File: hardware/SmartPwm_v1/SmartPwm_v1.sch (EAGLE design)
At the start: 12 parts, among them IC1 7805T, Q1 IRF3704-H, Q2 IRF3704-H, U1 ICL7667CPAZ

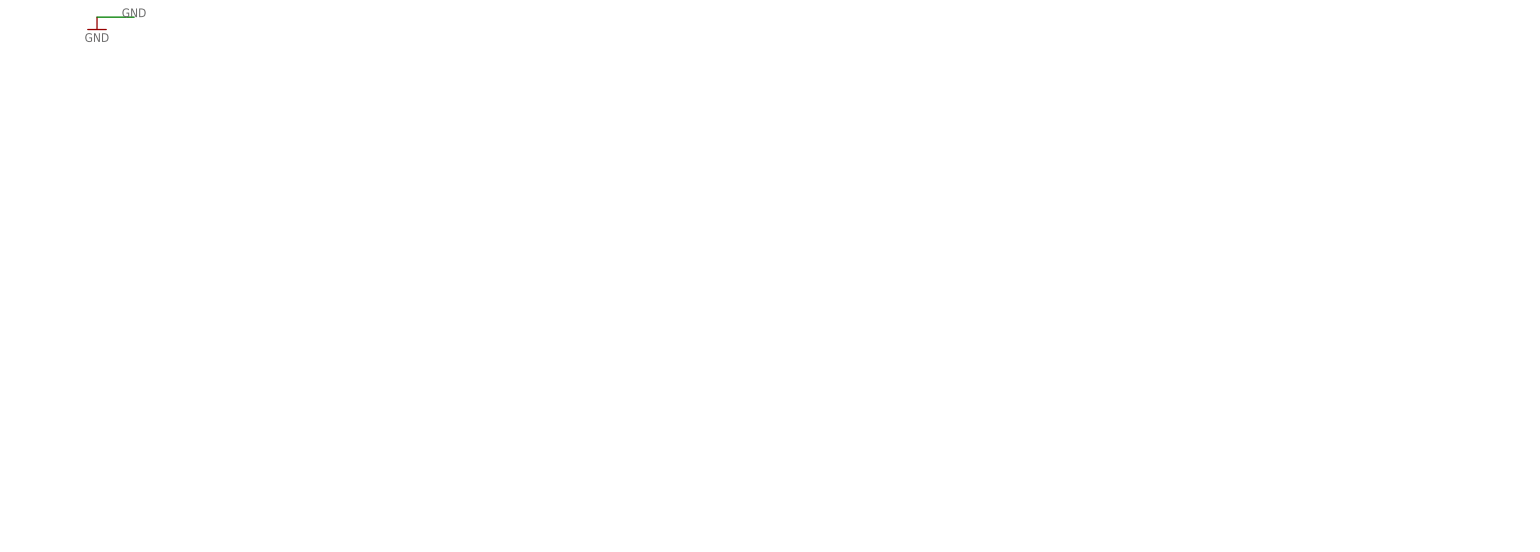
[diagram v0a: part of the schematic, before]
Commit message: add esp32 headers to shematic, add 4 control lines for pwm
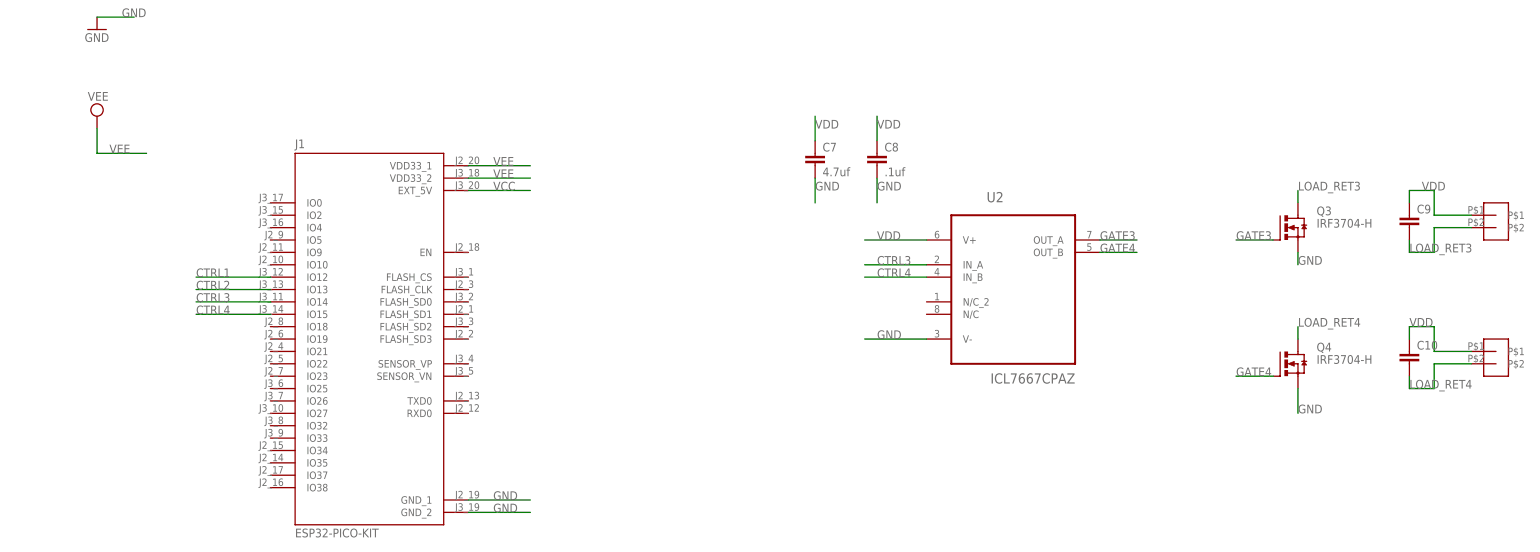
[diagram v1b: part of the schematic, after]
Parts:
- added C10, C9: (no value), capacitor-wima:C2.5/2
- added C7: 4.7uf, capacitor-wima:C2.5/2
- added C8: .1uf, capacitor-wima:C2.5/2
- added J1: ESP32-PICO-KIT, ESP32-PICO-KIT:ESP32-PICO-KIT
- added Q3, Q4: IRF3704-H, transistor-power:IRF3704-H
- added U$3, U$4: TB002-500-P02, mylib:TB002-500-P02
- added U2: ICL7667CPAZ, ICL7667CPAZ:ICL7667CPAZ
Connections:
- new net CTRL3: J1.IO14, U2.IN_A
- new net CTRL4: J1.IO15, U2.IN_B
- new net GATE3: Q3.G, U2.OUT_A
- new net GATE4: Q4.G, U2.OUT_B
- new net LOAD_RET3: C9.2, Q3.D, U$3.P$2
- new net LOAD_RET4: C10.2, Q4.D, U$4.P$2
- new net VEE: J1.VDD33_1, J1.VDD33_2
- net CTRL1: now also J1.IO12
- net CTRL2: now also J1.IO13
- net GND: now also C7.2, C8.2, J1.GND_1, J1.GND_2, Q3.S, Q4.S, U2.V-
- net VCC: now also J1.EXT_5V
- net VDD: now also C10.1, C7.1, C8.1, C9.1, U$3.P$1, U$4.P$1, U2.V+

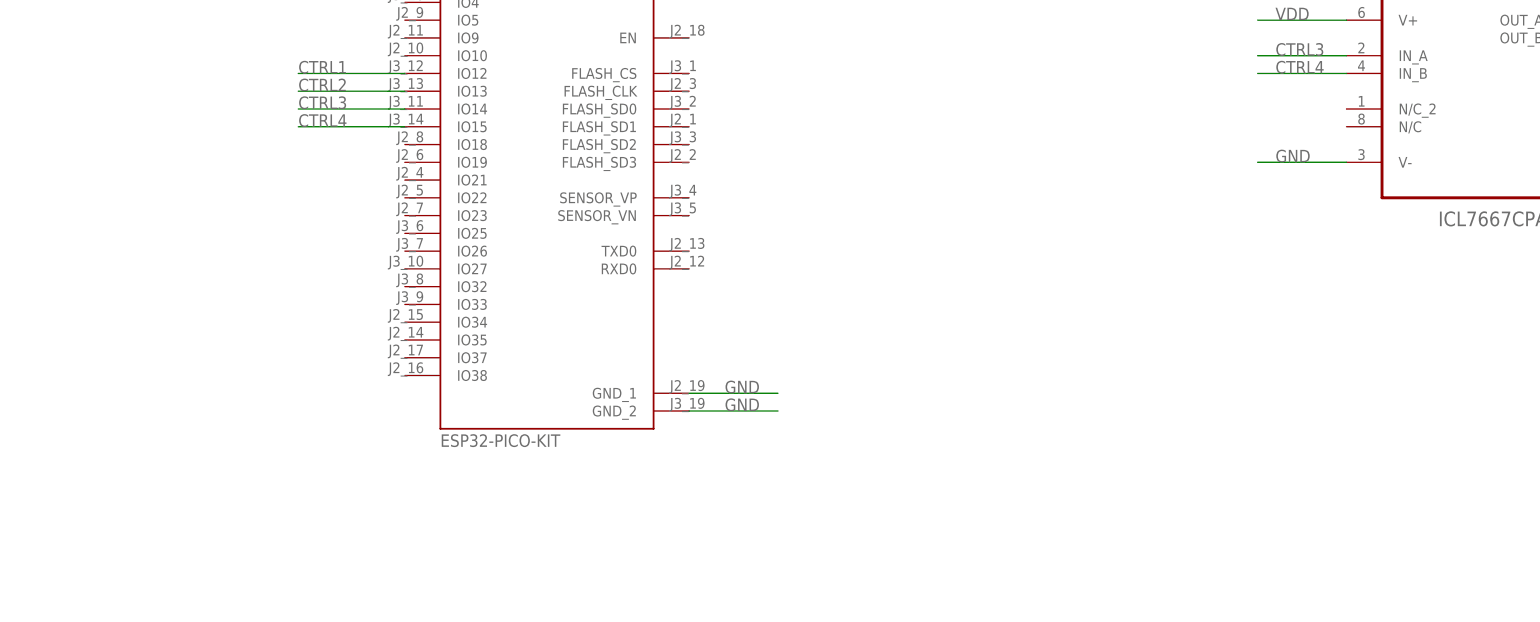
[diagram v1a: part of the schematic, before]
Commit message: Add header for IIC LCD display and add dht11 temp sensor
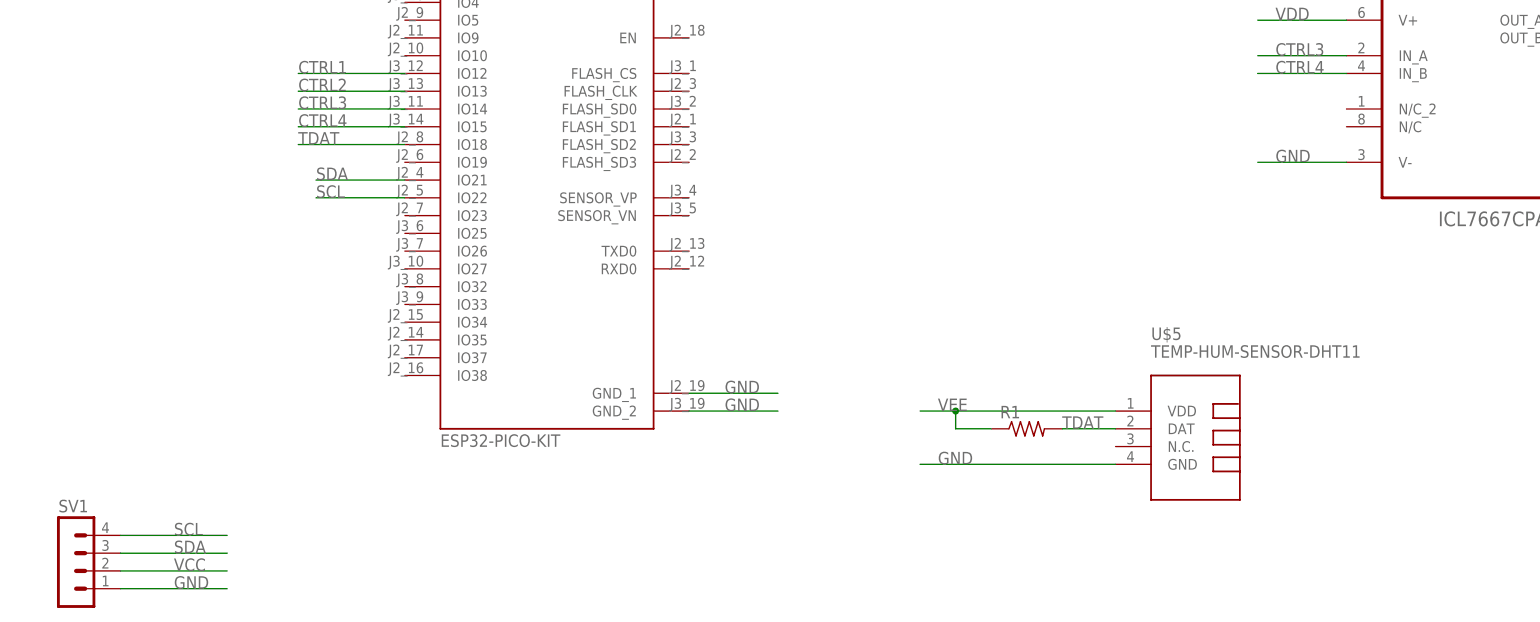
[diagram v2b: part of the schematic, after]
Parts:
- added R1: (no value), rcl:R-US_0207/10
- added SV1: (no value), con-lstb:MA04-1
- added U$5: TEMP-HUM-SENSOR-DHT11, diy-modules:TEMP-HUM-SENSOR-DHT11
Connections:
- new net SCL: J1.IO22, SV1.4
- new net SDA: J1.IO21, SV1.3
- new net TDAT: J1.IO18, R1.2, U$5.DAT
- net GND: now also SV1.1, U$5.GND
- net VCC: now also SV1.2
- net VEE: now also R1.1, U$5.VDD
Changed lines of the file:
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@@
 <layer number="97" name="Info" color="7" fill="1" visible="yes" active="yes"/>
 <layer number="98" name="Guide" color="6" fill="1" visible="yes" active="yes"/>
+<layer number="101" name="Hidden" color="15" fill="1" visible="yes" active="yes"/>
+<layer number="102" name="Changes" color="12" fill="1" visible="yes" active="yes"/>
 </layers>
 <schematic xreflabel="%F%N/%S.%C%R" xrefpart="/%S.%C%R">
@@
 <part name="C9" library="capacitor-wima" library_urn="urn:adsk.eagle:library:116" deviceset="C" device="2.5/2" package3d_urn="urn:adsk.eagle:package:5415/1"/>
 <part name="C10" library="capacitor-wima" library_urn="urn:adsk.eagle:library:116" deviceset="C" device="2.5/2" package3d_urn="urn:adsk.eagle:package:5415/1"/>
+<part name="SV1" library="con-lstb" library_urn="urn:adsk.eagle:library:162" deviceset="MA04-1" device="" package3d_urn="urn:adsk.eagle:package:8337/1"/>
+<part name="U$5" library="diy-modules" deviceset="TEMP-HUM-SENSOR-DHT11" device=""/>
+<part name="R1" library="rcl" library_urn="urn:adsk.eagle:library:334" deviceset="R-US_" device="0207/10" package3d_urn="urn:adsk.eagle:package:23491/2"/>
 </parts>
 <sheets>
@@
 <attribute name="VALUE" x="286.004" y="-22.479" size="1.778" layer="96"/>
 </instance>
+<instance part="SV1" gate="1" x="2.54" y="-71.12" smashed="yes">
+<attribute name="VALUE" x="1.27" y="-81.28" size="1.778" layer="96"/>
+<attribute name="NAME" x="1.27" y="-65.278" size="1.778" layer="95"/>
+</instance>
+<instance part="U$5" gate="G$1" x="165.1" y="-55.88" smashed="yes">
+<attribute name="NAME" x="157.48" y="-40.64" size="1.778" layer="95"/>
+<attribute name="VALUE" x="157.48" y="-43.18" size="1.778" layer="95"/>
+</instance>
+<instance part="R1" gate="G$1" x="139.7" y="-53.34" smashed="yes">
+<attribute name="NAME" x="135.89" y="-51.8414" size="1.778" layer="95"/>
+<attribute name="VALUE" x="135.89" y="-56.642" size="1.778" layer="96"/>
+</instance>
 </instances>
 <busses>
@@
 <label x="175.26" y="15.24" size="1.778" layer="95"/>
 </segment>
+<segment>
+<pinref part="SV1" gate="1" pin="1"/>
+<wire x1="10.16" y1="-76.2" x2="25.4" y2="-76.2" width="0.1524" layer="91"/>
+<label x="17.78" y="-76.2" size="1.778" layer="95"/>
+</segment>
+<segment>
+<pinref part="U$5" gate="G$1" pin="GND"/>
+<wire x1="152.4" y1="-58.42" x2="124.46" y2="-58.42" width="0.1524" layer="91"/>
+<label x="127" y="-58.42" size="1.778" layer="95"/>
+</segment>
 </net>
 <net name="VCC" class="0">
@@
 <pinref part="J1" gate="G$1" pin="EXT_5V"/>
 <label x="96.52" y="15.24" size="1.778" layer="95"/>
+</segment>
+<segment>
+<pinref part="SV1" gate="1" pin="2"/>
+<wire x1="10.16" y1="-73.66" x2="25.4" y2="-73.66" width="0.1524" layer="91"/>
+<label x="17.78" y="-73.66" size="1.778" layer="95"/>
 </segment>
 </net>
@@
 <label x="96.52" y="17.78" size="1.778" layer="95"/>
 </segment>
+<segment>
+<pinref part="U$5" gate="G$1" pin="VDD"/>
+<wire x1="152.4" y1="-50.8" x2="129.54" y2="-50.8" width="0.1524" layer="91"/>
+<pinref part="R1" gate="G$1" pin="1"/>
+<wire x1="134.62" y1="-53.34" x2="129.54" y2="-53.34" width="0.1524" layer="91"/>
+<wire x1="129.54" y1="-53.34" x2="129.54" y2="-50.8" width="0.1524" layer="91"/>
+<wire x1="129.54" y1="-50.8" x2="124.46" y2="-50.8" width="0.1524" layer="91"/>
+<junction x="129.54" y="-50.8"/>
+<label x="127" y="-50.8" size="1.778" layer="95"/>
+</segment>
 </net>
 <net name="CTRL4" class="0">
@@
 <wire x1="261.62" y1="12.7" x2="261.62" y2="15.24" width="0.1524" layer="91"/>
 <label x="261.62" y="15.24" size="1.778" layer="95"/>
+</segment>
+</net>
+<net name="SCL" class="0">
+<segment>
+<pinref part="SV1" gate="1" pin="4"/>
+<wire x1="10.16" y1="-68.58" x2="25.4" y2="-68.58" width="0.1524" layer="91"/>
+<label x="17.78" y="-68.58" size="1.778" layer="95"/>
+</segment>
+<segment>
+<pinref part="J1" gate="G$1" pin="IO22"/>
+<wire x1="50.8" y1="-20.32" x2="38.1" y2="-20.32" width="0.1524" layer="91"/>
+<label x="38.1" y="-20.32" size="1.778" layer="95"/>
+</segment>
+</net>
+<net name="SDA" class="0">
+<segment>
+<pinref part="SV1" gate="1" pin="3"/>
+<wire x1="10.16" y1="-71.12" x2="25.4" y2="-71.12" width="0.1524" layer="91"/>
+<label x="17.78" y="-71.12" size="1.778" layer="95"/>
+</segment>
+<segment>
+<pinref part="J1" gate="G$1" pin="IO21"/>
+<wire x1="50.8" y1="-17.78" x2="38.1" y2="-17.78" width="0.1524" layer="91"/>
+<label x="38.1" y="-17.78" size="1.778" layer="95"/>
+</segment>
+</net>
+<net name="TDAT" class="0">
+<segment>
+<pinref part="U$5" gate="G$1" pin="DAT"/>
+<pinref part="R1" gate="G$1" pin="2"/>
+<wire x1="152.4" y1="-53.34" x2="144.78" y2="-53.34" width="0.1524" layer="91"/>
+<label x="144.78" y="-53.34" size="1.778" layer="95"/>
+</segment>
+<segment>
+<pinref part="J1" gate="G$1" pin="IO18"/>
+<wire x1="50.8" y1="-12.7" x2="35.56" y2="-12.7" width="0.1524" layer="91"/>
+<label x="35.56" y="-12.7" size="1.778" layer="95"/>
 </segment>
 </net>
@@
 packages will not be understood (or retained) with this version.
 </note>
+<note version="8.4" severity="warning">
+Since Version 8.4, EAGLE supports properties for SPICE simulation.
+Probes in schematics and SPICE mapping objects found in parts and library devices
+will not be understood with this version. Update EAGLE to the latest version
+for full support of SPICE simulation.
+</note>
 </compatibility>

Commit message: add knobs to schematic, rearrange ios, select lcd and add to docs
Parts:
- added MT1, MT2, MT3, MT4, MT5: PEC11R-4215F-S0024, PEC11R-4215F-S0024:PEC11R-4215F-S0024
- added R2: 10M, rcl:R-US_0207/10
- added R3: 1M, rcl:R-US_0207/10
- added R4, R5: 10K, rcl:R-US_0207/10
- added SV2: (no value), con-lstb:MA04-1
- added U$6: 74AHTC125, DIP794W45P254L1969H508Q14:74AHTC125
- C10, C5, C6, C9: value (none) -> 10uf
- R1: value (none) -> 10K
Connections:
- new net K1_A: J1.IO2, MT1.A
- new net K1_B: J1.IO5, MT1.B
- new net K1_S: J1.IO0, MT1.2
- new net K2_A: J1.IO26, MT2.A
- new net K2_B: J1.IO10, MT2.B
- new net K2_S: J1.IO4, MT2.2
- new net K3_A: J1.IO32, MT3.A
- new net K3_B: J1.IO9, MT3.B
- new net K3_S: J1.IO27, MT3.2
- new net K4_A: J1.IO35, MT4.A
- new net K4_B: MT4.B
- new net K4_S: J1.IO34, MT4.2
- new net K5_A: J1.IO33, MT5.A
- new net K5_B: J1.IO25, MT5.B
- new net K5_S: J1.IO37, MT5.2
- new net LDAT3V3: J1.IO19, U$6.1A
- new net LDAT5V: SV2.2, SV2.3, U$6.1Y
- new net VDIV: J1.IO38, R2.1, R3.2
- net GND: now also MT1.1, MT1.COM, MT1.SHIELD, MT2.1, MT2.COM, MT2.SHIELD, MT3.1, MT3.COM, MT3.SHIELD, MT4.1, MT4.COM, MT4.SHIELD, MT5.1, MT5.COM, MT5.SHIELD, R3.1, SV2.1, U$6.1OE_N, U$6.2A, U$6.3A, U$6.GND
- net SCL: now also R4.2
- net SDA: now also R5.2
- net VCC: now also U$6.2OE_N, U$6.3OE_N, U$6.4A, U$6.4OE_N, U$6.VCC; no longer SV1.2
- net VDD: now also R2.2, SV2.4
- net VEE: now also R4.1, R5.1, SV1.2
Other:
- note added: "ADC_CH2"
- note added: "LCD Display"
- note added: "Optional pullups, do not populate if not needed"
- note added: "PWM Outputs"
- note added: "Power Monitor"
- note added: "RTC_GPIO"
- note added: "Temperature"
- note added: "VEE = 3v3"
- note added: "knobs"
- note added: "lowimpedance"
- note added: "tantalum"
- note added: "ws2815"

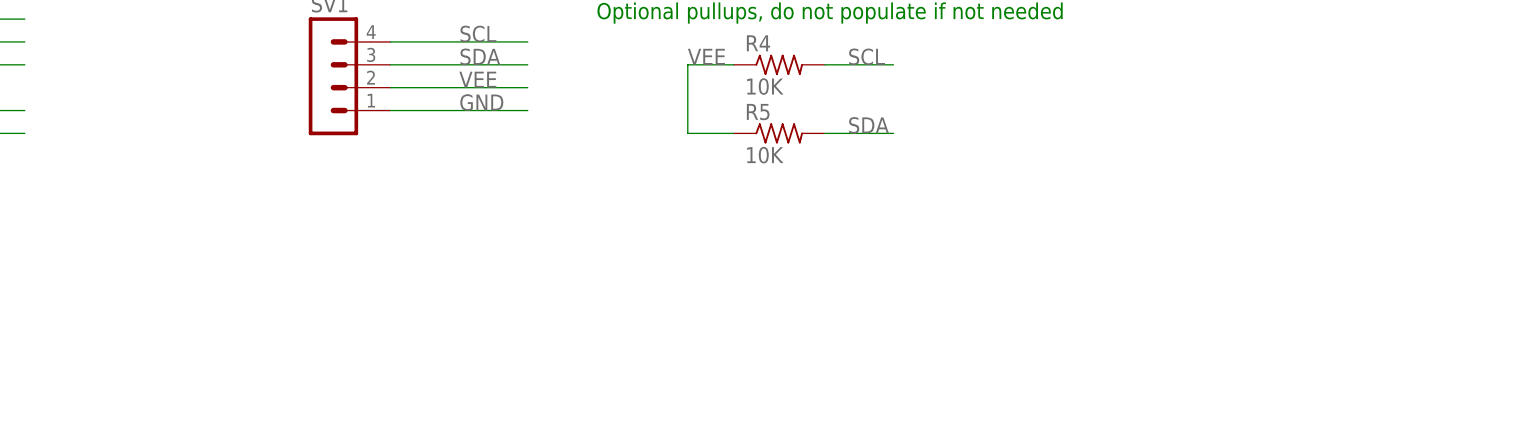
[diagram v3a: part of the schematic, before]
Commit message: add optional grove connector for IIC bus
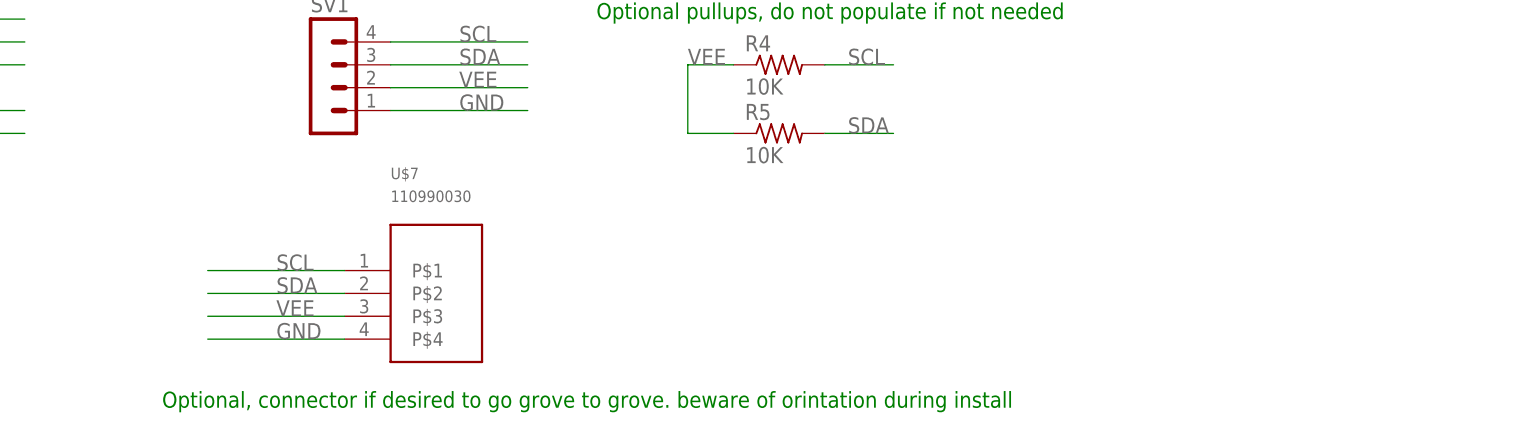
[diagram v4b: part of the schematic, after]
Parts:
- added U$7: 110990030, seeedgrove:110990030
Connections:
- net GND: now also U$7.P$4
- net SCL: now also U$7.P$1
- net SDA: now also U$7.P$2
- net VEE: now also U$7.P$3
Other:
- note added: "Optional, connector if desired to go grove to grove. beware of orintation during install"
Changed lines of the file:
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@@
 <part name="R4" library="rcl" library_urn="urn:adsk.eagle:library:334" deviceset="R-US_" device="0207/10" package3d_urn="urn:adsk.eagle:package:23491/2" value="10K"/>
 <part name="R5" library="rcl" library_urn="urn:adsk.eagle:library:334" deviceset="R-US_" device="0207/10" package3d_urn="urn:adsk.eagle:package:23491/2" value="10K"/>
+<part name="U$7" library="seeedgrove" deviceset="110990030" device=""/>
 </parts>
 <sheets>
@@
 <text x="182.88" y="20.32" size="1.778" layer="91">lowimpedance</text>
 <text x="33.02" y="-66.04" size="1.778" layer="91">Optional pullups, do not populate if not needed</text>
+<text x="-15.24" y="-109.22" size="1.778" layer="91">Optional, connector if desired to go grove to grove. beware of orintation during install</text>
 </plain>
 <instances>
@@
 <attribute name="VALUE" x="49.53" y="-82.042" size="1.778" layer="96"/>
 </instance>
+<instance part="U$7" gate="G$1" x="35.56" y="-101.6" smashed="yes">
+<attribute name="NAME" x="10.16" y="-83.82" size="1.27" layer="95"/>
+<attribute name="VALUE" x="10.16" y="-86.36" size="1.27" layer="96"/>
+</instance>
 </instances>
 <busses>
@@
 <wire x1="33.02" y1="129.54" x2="50.8" y2="129.54" width="0.1524" layer="91"/>
 <label x="38.1" y="129.54" size="1.778" layer="95"/>
+</segment>
+<segment>
+<wire x1="-10.16" y1="-101.6" x2="5.08" y2="-101.6" width="0.1524" layer="91"/>
+<label x="-2.54" y="-101.6" size="1.778" layer="95"/>
+<pinref part="U$7" gate="G$1" pin="P$4"/>
 </segment>
 </net>
@@
 <label x="43.18" y="-71.12" size="1.778" layer="95"/>
 </segment>
+<segment>
+<wire x1="-10.16" y1="-99.06" x2="5.08" y2="-99.06" width="0.1524" layer="91"/>
+<label x="-2.54" y="-99.06" size="1.778" layer="95"/>
+<pinref part="U$7" gate="G$1" pin="P$3"/>
+</segment>
 </net>
 <net name="CTRL4" class="0">
@@
 <label x="60.96" y="-71.12" size="1.778" layer="95"/>
 </segment>
+<segment>
+<wire x1="-10.16" y1="-93.98" x2="5.08" y2="-93.98" width="0.1524" layer="91"/>
+<label x="-2.54" y="-93.98" size="1.778" layer="95"/>
+<pinref part="U$7" gate="G$1" pin="P$1"/>
+</segment>
 </net>
 <net name="SDA" class="0">
@@
 <label x="60.96" y="-78.74" size="1.778" layer="95"/>
 </segment>
-</net>
+<segment>
+<wire x1="-10.16" y1="-96.52" x2="5.08" y2="-96.52" width="0.1524" layer="91"/>
+<label x="-2.54" y="-96.52" size="1.778" layer="95"/>
+<pinref part="U$7" gate="G$1" pin="P$2"/>
+</segment>
+</net>
